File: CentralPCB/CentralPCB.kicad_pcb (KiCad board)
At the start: 2 copper layers, 56 parts, among them J1 POWER HEADER, J2 SPI Header, J3 Conn_02x16_Odd_Even, J4 MIDI IN, J5 MIDI OUT, J6 DAC Comm, U1 AD8531, U2 Teensy4.1, U3 BA7810CP-E2

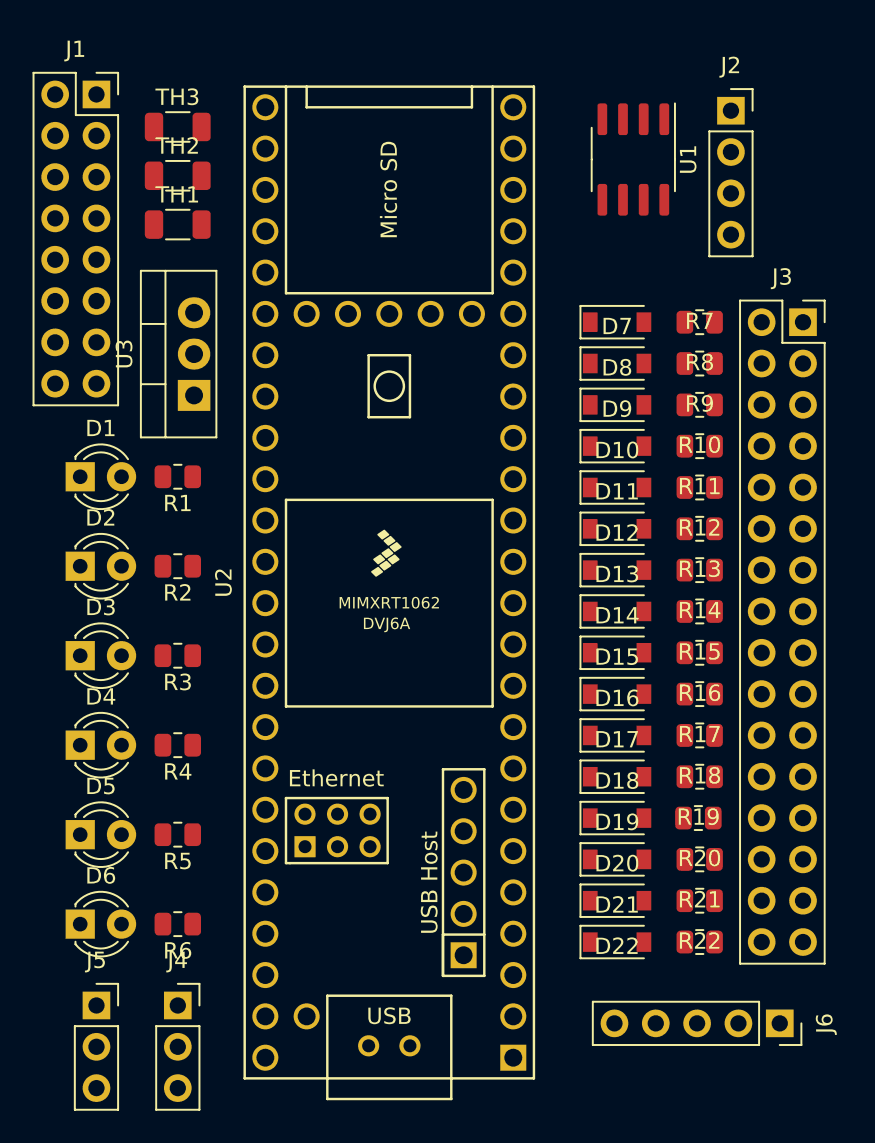
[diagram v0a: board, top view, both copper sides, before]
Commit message: Fixed Teensy connections
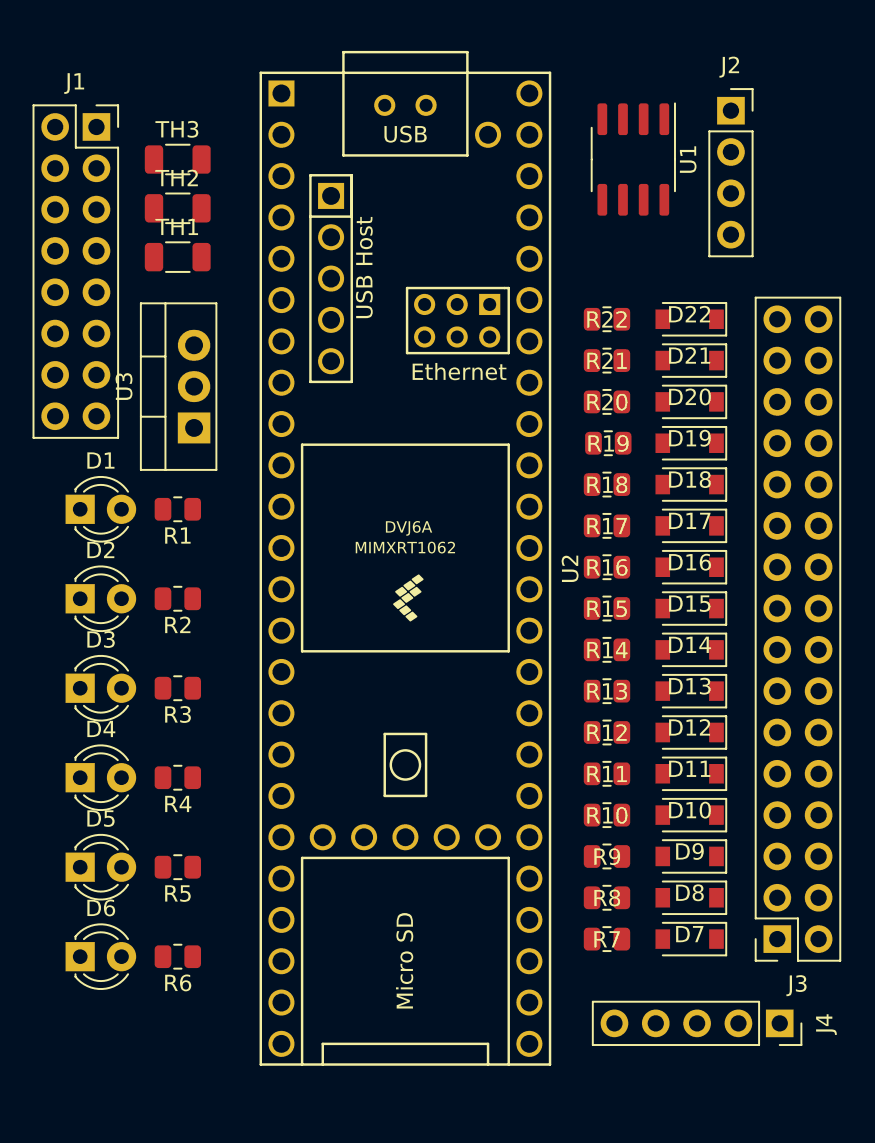
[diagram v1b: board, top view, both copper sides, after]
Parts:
- removed the J4 at (24.1, 72.5)
- removed J5: MIDI OUT, Connector_PinSocket_2.54mm:PinSocket_1x03_P2.54mm_Vertical
- moved R22 38.7 mm to (50.4, 30.3), turned to 180 degrees
- moved D22 38.5 mm to (55.5, 30.3), turned to 180 degrees
- moved R7 38.3 mm to (50.4, 68.4), turned to 180 degrees
- moved D7 38.2 mm to (55.5, 68.4), turned to 180 degrees
- moved J3 38.0 mm to (60.9, 68.4), turned to 180 degrees
- moved R21 33.7 mm to (50.4, 32.9), turned to 180 degrees
- moved D21 33.5 mm to (55.5, 32.9), turned to 180 degrees
- moved R8 33.3 mm to (50.4, 65.9), turned to 180 degrees
- moved D8 33.1 mm to (55.5, 65.9), turned to 180 degrees
- moved R20 28.7 mm to (50.4, 35.4), turned to 180 degrees
- moved D20 28.5 mm to (55.5, 35.4), turned to 180 degrees
- moved R9 28.3 mm to (50.4, 63.4), turned to 180 degrees
- moved D9 28.1 mm to (55.5, 63.4), turned to 180 degrees
- moved R19 23.7 mm to (50.5, 38.0), turned to 180 degrees
- moved D19 23.5 mm to (55.5, 38.0), turned to 180 degrees
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- renumbered J6 to J4
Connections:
- net Net-(U2-Pad18) renamed MOSI1
- net Net-(U2-Pad19) renamed SCK1
- net Net-(U2-Pad2) renamed CS1
- net Net-(U2-Pad3) renamed MISO1
- net Net-(U2-Pad9) renamed MIDIREC
- J3 pad 13: +5V -> +3V3
- J3 pad 15: +5V -> +3V3
- J3 pad 19: +3V3 -> Net-(J3-Pad19)
- J3 pad 21: +3V3 -> Net-(J3-Pad21)
- J3 pad 23: +3V3 -> MIDREC
- J3 pad 25: GND -> MIDITRANS
- J3 pad 7: +12V -> +5V
- U2 pad 1: Net-(U2-Pad1) -> GND
- U2 pad 10: Net-(U2-Pad10) -> MIDITRANS
- U2 pad 12: Net-(U2-Pad12) -> CS0
- U2 pad 13: Net-(U2-Pad13) -> MOSI0
- U2 pad 14: Net-(U2-Pad14) -> MISO0
- U2 pad 16: Net-(U2-Pad16) -> DC3
- U2 pad 17: Net-(U2-Pad17) -> DC4
- U2 pad 30: Net-(U2-Pad30) -> DD1
- U2 pad 31: Net-(U2-Pad31) -> DD2
- U2 pad 32: Net-(U2-Pad32) -> DD3
- U2 pad 33: Net-(U2-Pad33) -> DD4
- U2 pad 34: Net-(U2-Pad34) -> GND
- U2 pad 35: Net-(U2-Pad35) -> SCK0
- U2 pad 36: Net-(U2-Pad36) -> DA1
- U2 pad 37: Net-(U2-Pad37) -> DA2
- U2 pad 38: Net-(U2-Pad38) -> DA3
- U2 pad 39: Net-(U2-Pad39) -> DA4
- U2 pad 4: Net-(U2-Pad4) -> Net-(R3-Pad1)
- U2 pad 40: Net-(U2-Pad40) -> DB1
- U2 pad 41: Net-(U2-Pad41) -> DB2
- U2 pad 42: Net-(U2-Pad42) -> DB3
- U2 pad 43: Net-(U2-Pad43) -> DB4
- U2 pad 44: Net-(U2-Pad44) -> DC1
- U2 pad 45: Net-(U2-Pad45) -> DC2
- U2 pad 46: Net-(U2-Pad46) -> Net-(U1-Pad3)
- U2 pad 47: Net-(U2-Pad47) -> GND
- U2 pad 48: Net-(U2-Pad48) -> +5V
- U2 pad 5: Net-(U2-Pad5) -> Net-(R4-Pad1)
- U2 pad 52: Net-(U2-Pad52) -> GND
- U2 pad 58: Net-(U2-Pad58) -> GND
- U2 pad 59: Net-(U2-Pad59) -> GND
- U2 pad 6: Net-(U2-Pad6) -> Net-(R5-Pad1)
- U2 pad 64: Net-(U2-Pad64) -> GND
- U2 pad 7: Net-(U2-Pad7) -> Net-(R6-Pad1)

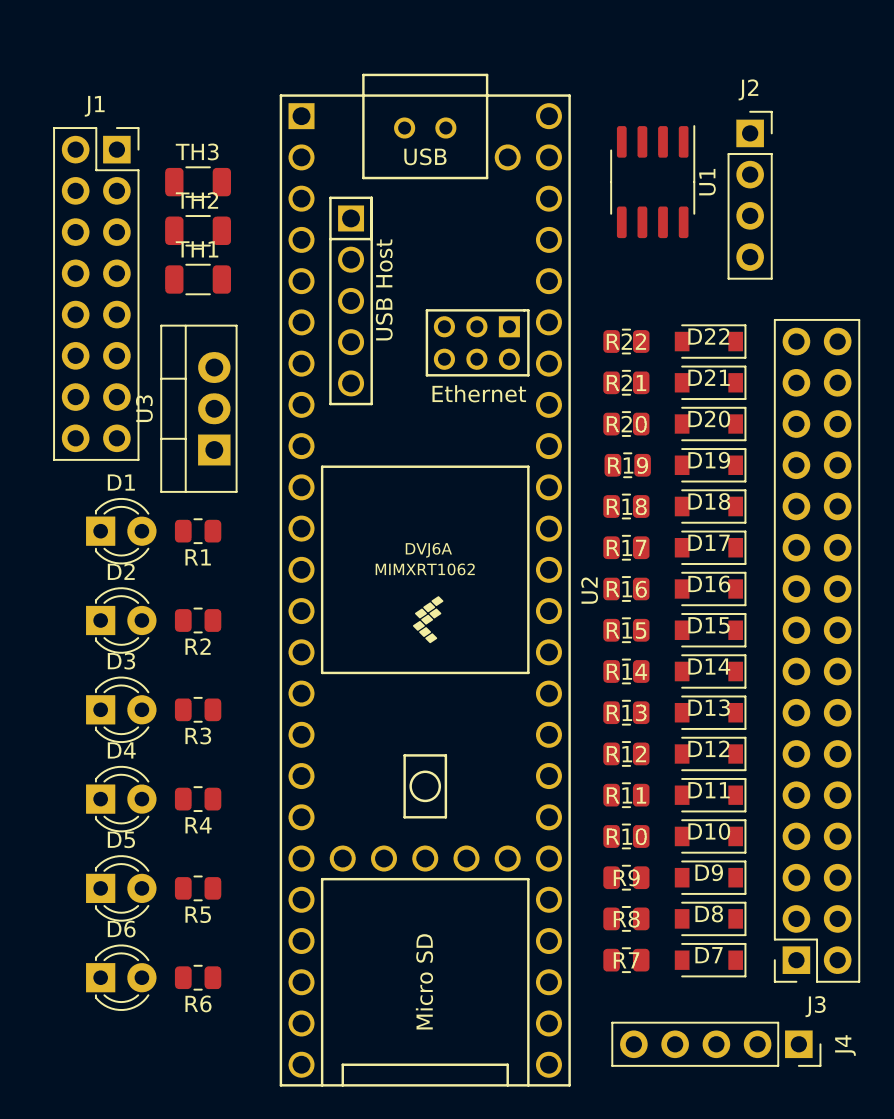
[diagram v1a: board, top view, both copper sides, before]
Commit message: Consolidated pin headers
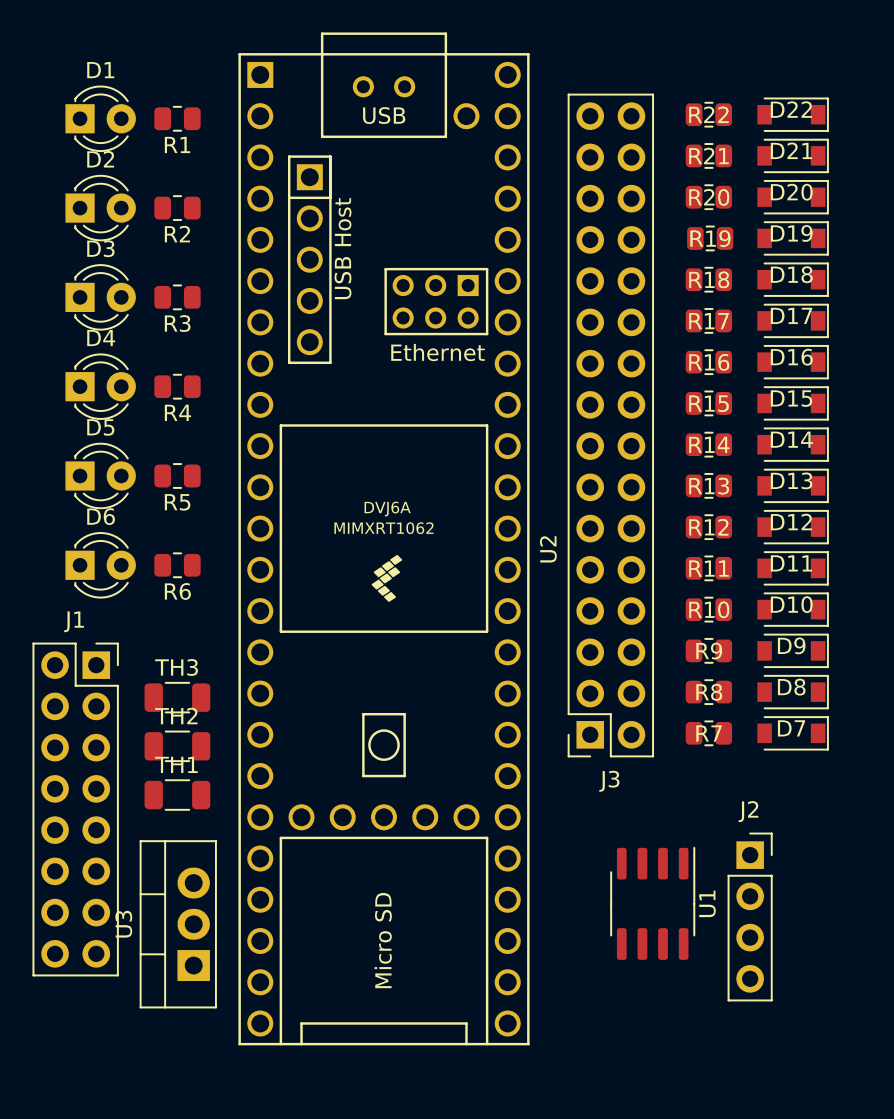
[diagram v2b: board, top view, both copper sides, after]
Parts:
- removed J4: DAC Comm, Connector_PinSocket_2.54mm:PinSocket_1x05_P2.54mm_Vertical
- moved J2 44.5 mm to (58.0, 62.0)
- moved U1 44.4 mm to (52.0, 65.0)
- moved U3 31.8 mm to (23.8, 68.8)
- moved J1 31.8 mm to (17.8, 50.3)
- moved TH1 31.8 mm to (22.8, 58.3)
- moved TH2 31.8 mm to (22.8, 55.3)
- moved TH3 31.8 mm to (22.8, 52.3)
- moved D5 25.4 mm to (16.8, 38.6)
- moved D6 25.4 mm to (16.8, 44.1)
- moved R5 25.4 mm to (22.8, 38.6)
- moved R6 25.4 mm to (22.8, 44.1)
- moved D1 25.4 mm to (16.8, 16.6)
- moved D2 25.4 mm to (16.8, 22.1)
- moved D3 25.4 mm to (16.8, 27.6)
- moved D4 25.4 mm to (16.8, 33.1)
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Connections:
- J2 pad 1: CS0 -> CS1
- J2 pad 2: MOSI0 -> MOSI1
- J2 pad 3: MISO0 -> MISO1
- J2 pad 4: SCK0 -> SCK1
- J3 pad 11: +5V -> Net-(J3-Pad11)
- J3 pad 13: +3V3 -> Net-(J3-Pad13)
- J3 pad 15: +3V3 -> DisplayTX
- J3 pad 17: +3V3 -> DisplayRX
- J3 pad 19: Net-(J3-Pad19) -> CS0
- J3 pad 21: Net-(J3-Pad21) -> MOSI0
- J3 pad 23: MIDREC -> MISO0
- J3 pad 25: MIDITRANS -> SCK0
- J3 pad 27: GND -> MIDREC
- J3 pad 29: GND -> MIDITRANS
- J3 pad 3: +12V -> +10V
- J3 pad 5: +12V -> +5V
- J3 pad 7: +5V -> +3V3
- J3 pad 9: +5V -> Net-(J3-Pad9)

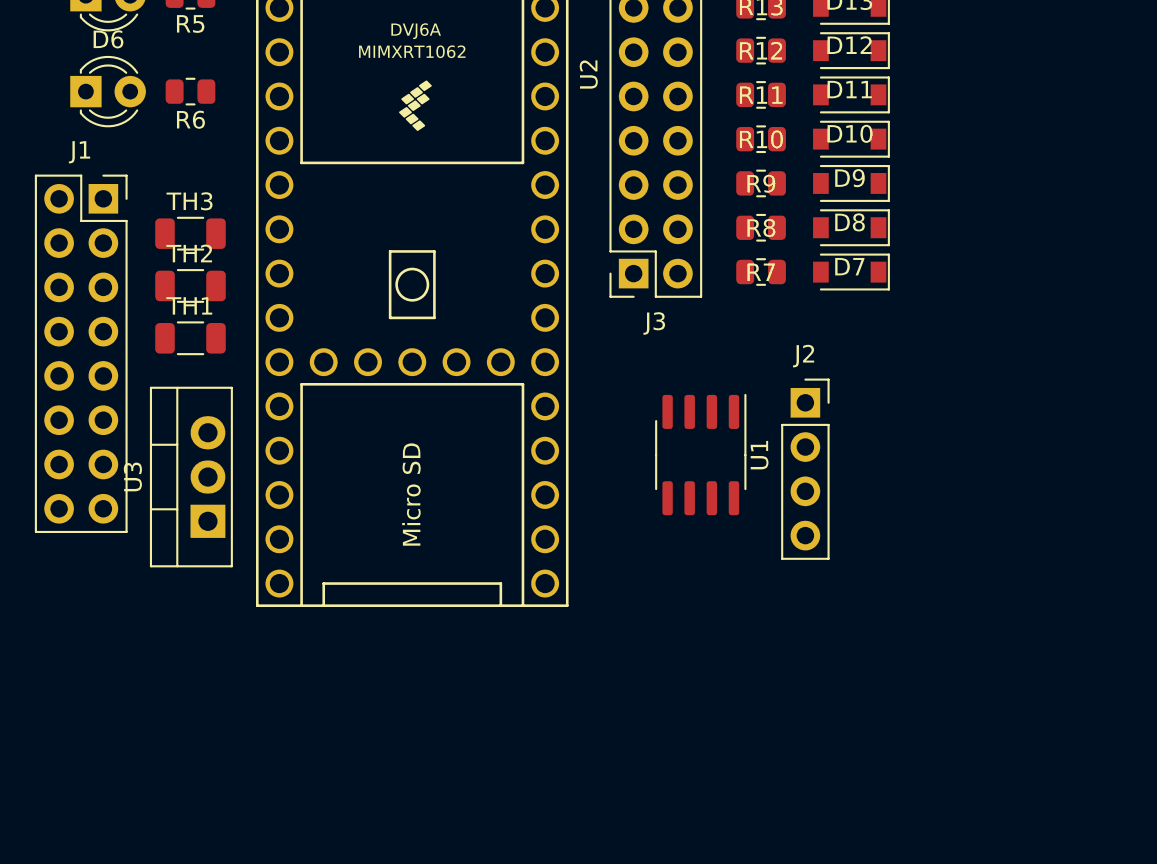
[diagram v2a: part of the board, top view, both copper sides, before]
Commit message: Updated DAC connections
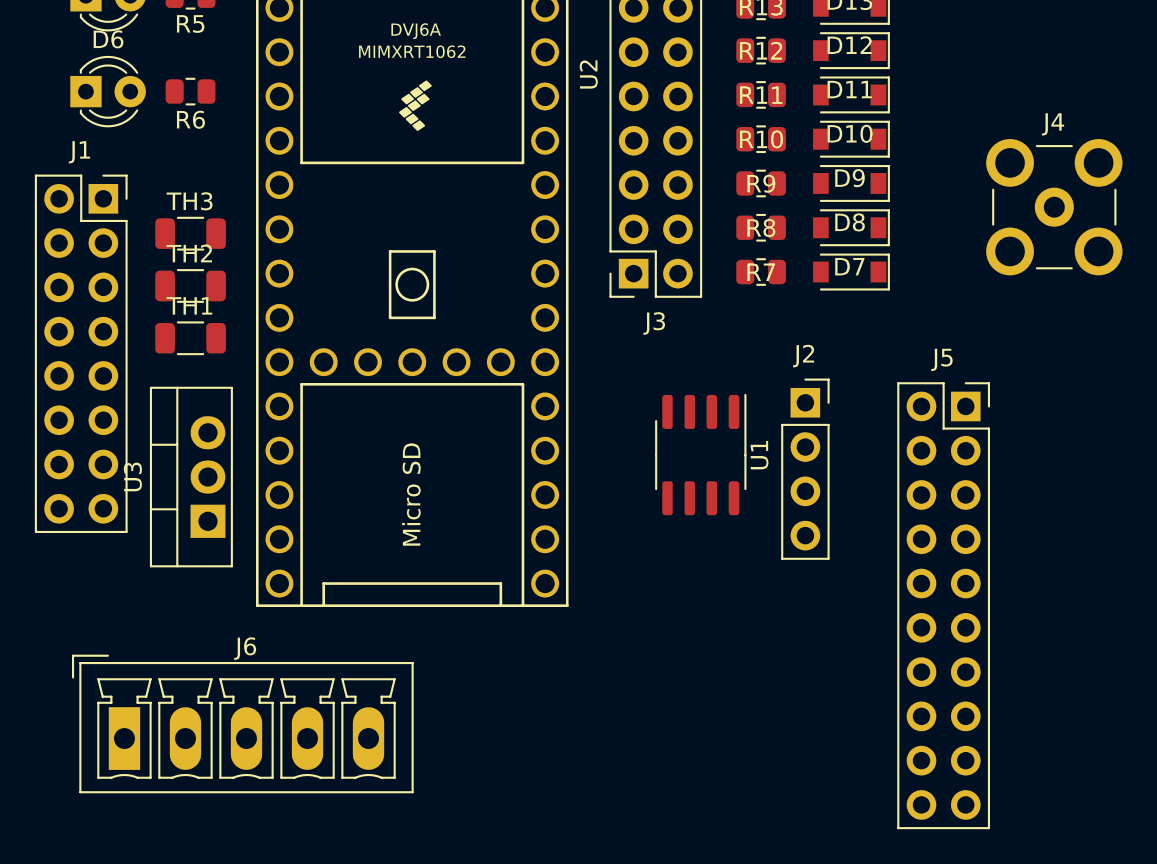
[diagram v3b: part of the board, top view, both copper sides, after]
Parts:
- added J4: Conn_Coaxial, Connector_Coaxial:SMB_Jack_Vertical, F.Cu at (72.3, 50.7)
- added J5: Conn_02x10_Odd_Even, Connector_PinSocket_2.54mm:PinSocket_2x10_P2.54mm_Vertical, F.Cu at (67.2, 62.2)
- added J6: Conn_01x05, Connectors_Phoenix:PhoenixContact_MCV-G_05x3.50mm_Vertical, F.Cu at (19.0, 81.2)
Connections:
- J2 pad 1: CS1 -> SCK0
- J2 pad 2: MOSI1 -> MISO0
- J2 pad 3: MISO1 -> MOSI0
- J2 pad 4: SCK1 -> CS0
- J3 pad 11: Net-(J3-Pad11) -> +3V3
- J3 pad 13: Net-(J3-Pad13) -> SCL
- J3 pad 15: DisplayTX -> SDA
- J3 pad 17: DisplayRX -> MIDREC
- J3 pad 19: CS0 -> MIDITRANS
- J3 pad 21: MOSI0 -> GND
- J3 pad 23: MISO0 -> GND
- J3 pad 25: SCK0 -> GND
- J3 pad 27: MIDREC -> GND
- J3 pad 29: MIDITRANS -> GND
- J3 pad 3: +10V -> +12V
- J3 pad 7: +3V3 -> +5V
- J3 pad 9: Net-(J3-Pad9) -> +3V3
- U2 pad 16: DC3 -> DC1
- U2 pad 17: DC4 -> DC2
- U2 pad 18: MOSI1 -> DC3
- U2 pad 19: SCK1 -> DC4
- U2 pad 2: CS1 -> LDAC
- U2 pad 3: MISO1 -> CLR
- U2 pad 40: DB1 -> SDA
- U2 pad 41: DB2 -> SCL
- U2 pad 42: DB3 -> DB1
- U2 pad 43: DB4 -> DB2
- U2 pad 44: DC1 -> DB3
- U2 pad 45: DC2 -> DB4
- U2 pad 8: Net-(U2-Pad8) -> RESET

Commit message: Pin updates
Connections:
- U2 pad 2: LDAC -> Net-(U2-Pad2)
- U2 pad 22: Net-(U2-Pad22) -> RESET
- U2 pad 23: Net-(U2-Pad23) -> LDAC
- U2 pad 24: Net-(U2-Pad24) -> CLR
- U2 pad 3: CLR -> Net-(U2-Pad3)
- U2 pad 8: RESET -> Net-(U2-Pad8)
